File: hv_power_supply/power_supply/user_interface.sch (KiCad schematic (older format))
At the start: 28 parts, among them SW1? EMS22A50-B28-LS6

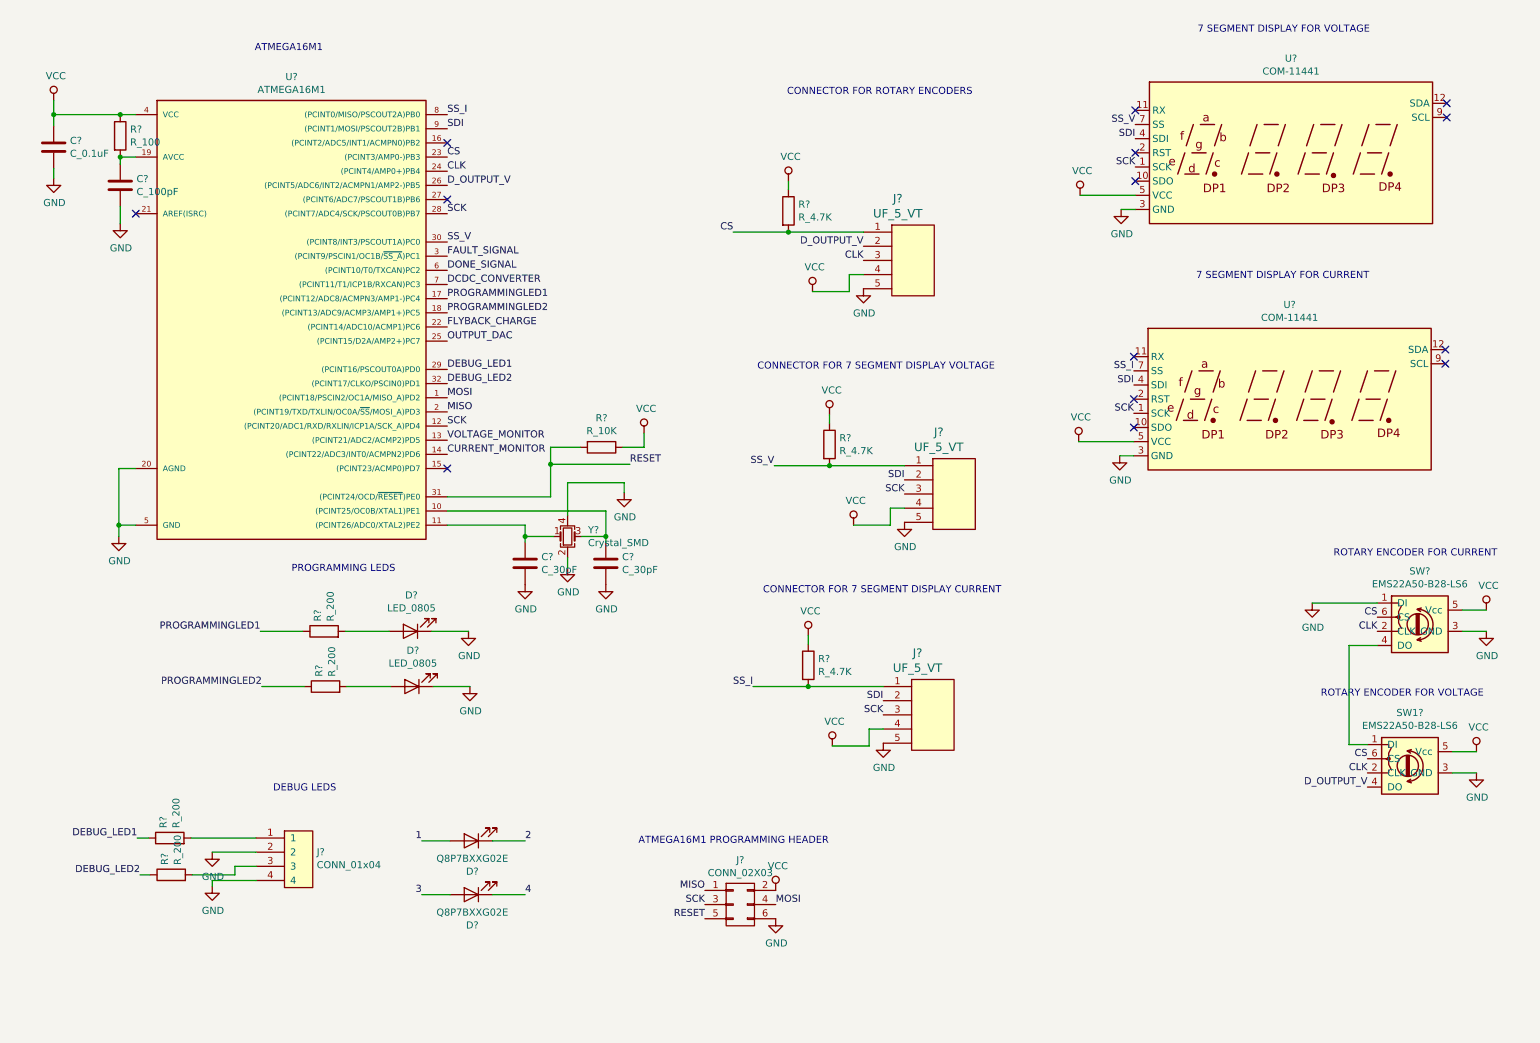
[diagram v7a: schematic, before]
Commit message: start text box
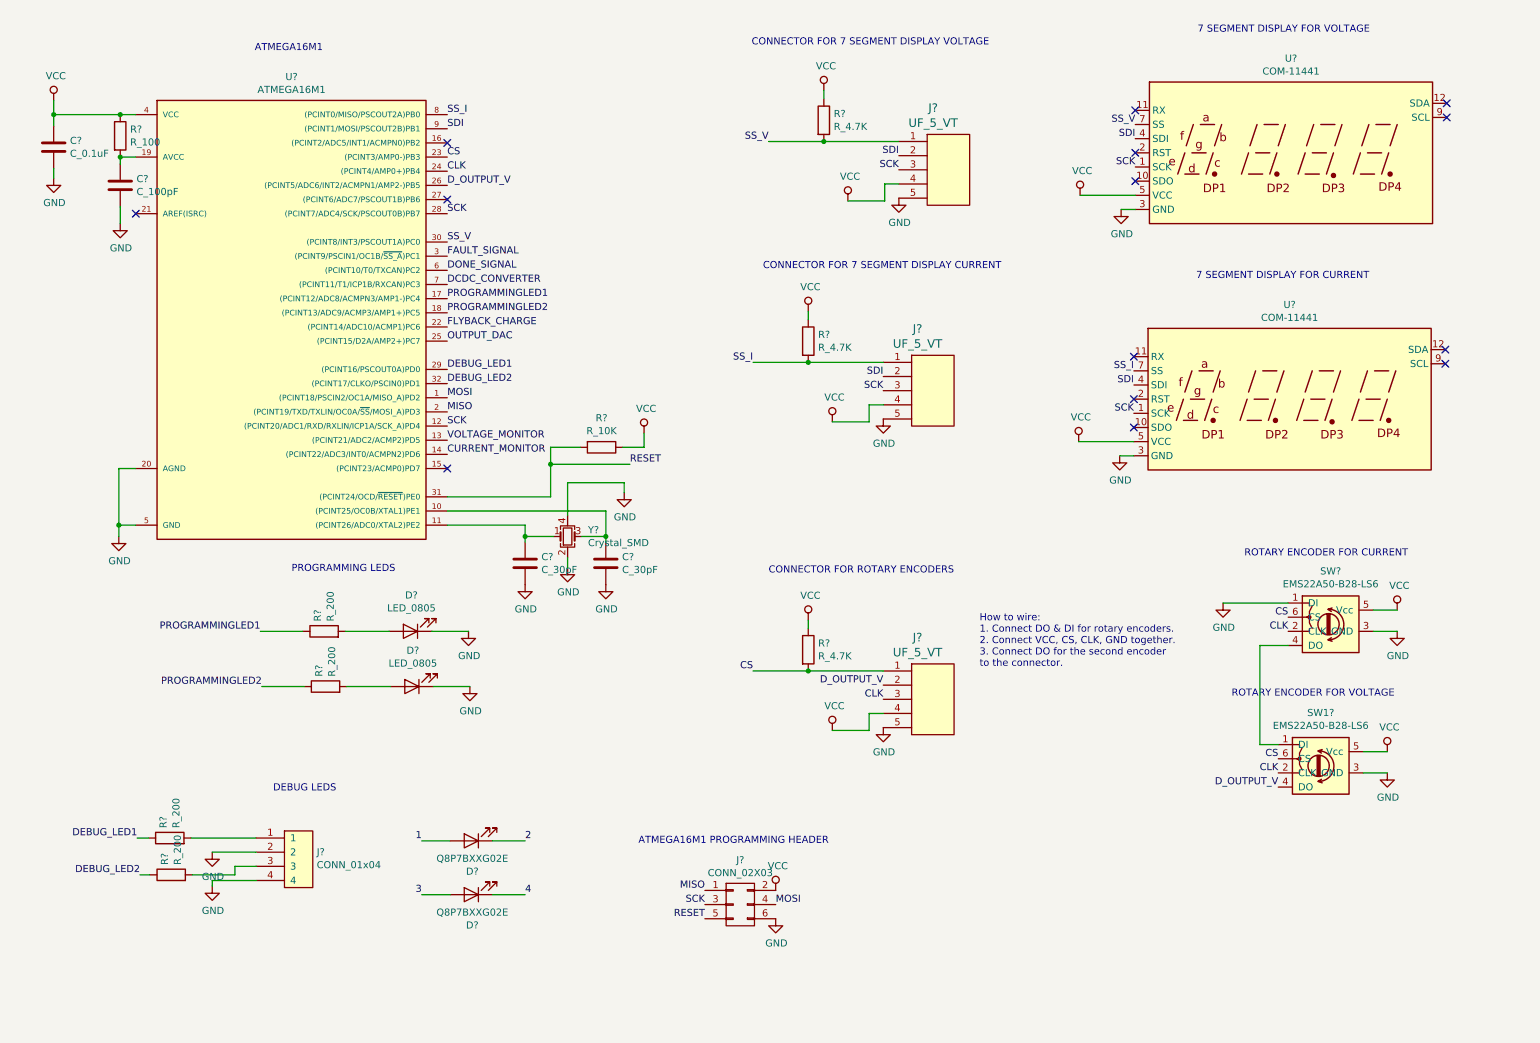
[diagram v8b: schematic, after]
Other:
- note added: "How to wire:\n1. Connect DO & DI for rotary encoders. \n2. Connect VCC, CS, CLK, GND together.\n3. Connect DO for the second encoder\nto the connector."
- moved on the sheet: J?, R?, SW1?, SW?
